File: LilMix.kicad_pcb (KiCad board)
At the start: 2 copper layers, 79.6 x 94.4 mm, 60 parts, among them J1_L1 MONO, J1_R1 MONO, J2_L1 MONO, J2_R1 MONO, J3 STEREO, J4 MONO, J5 MONO, J6 STEREO, U1 TL074, U2 NE5532

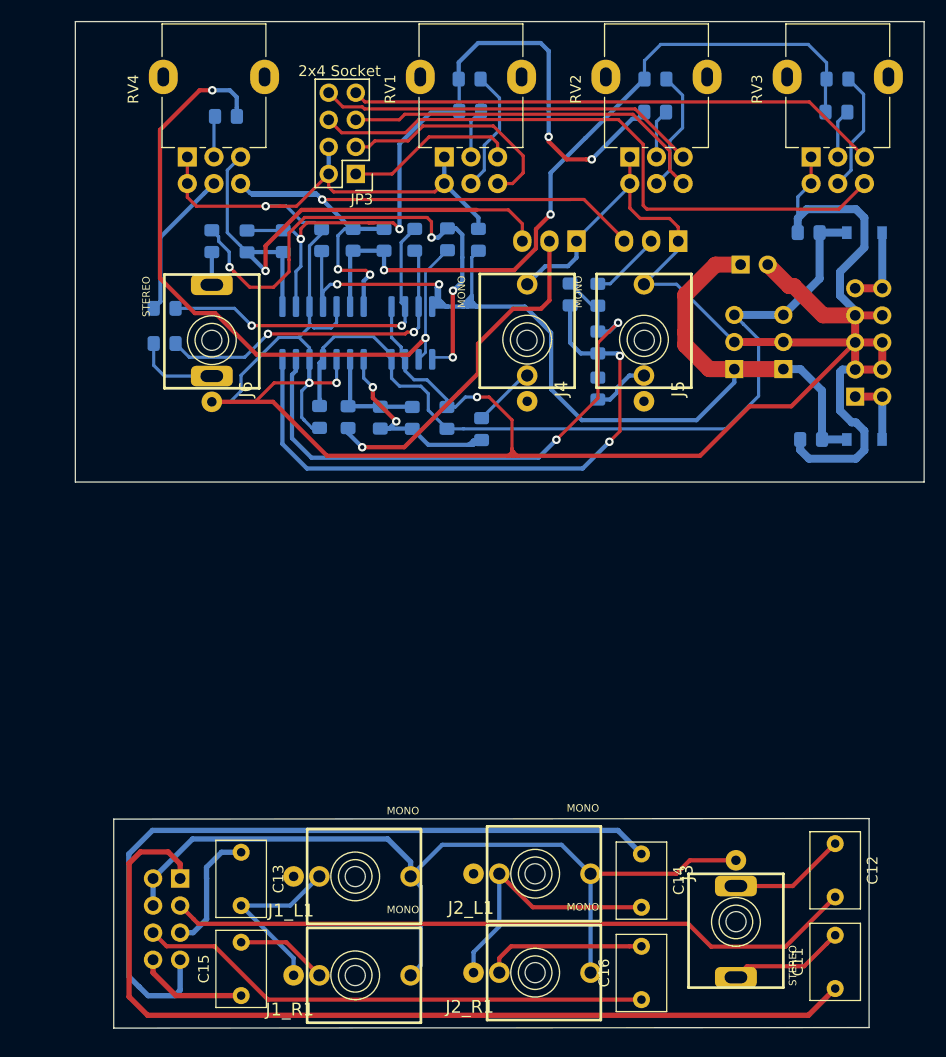
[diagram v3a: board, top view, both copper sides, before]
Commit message: Fixed jack destinatios and flipped front board orientation. Rerouted pcb
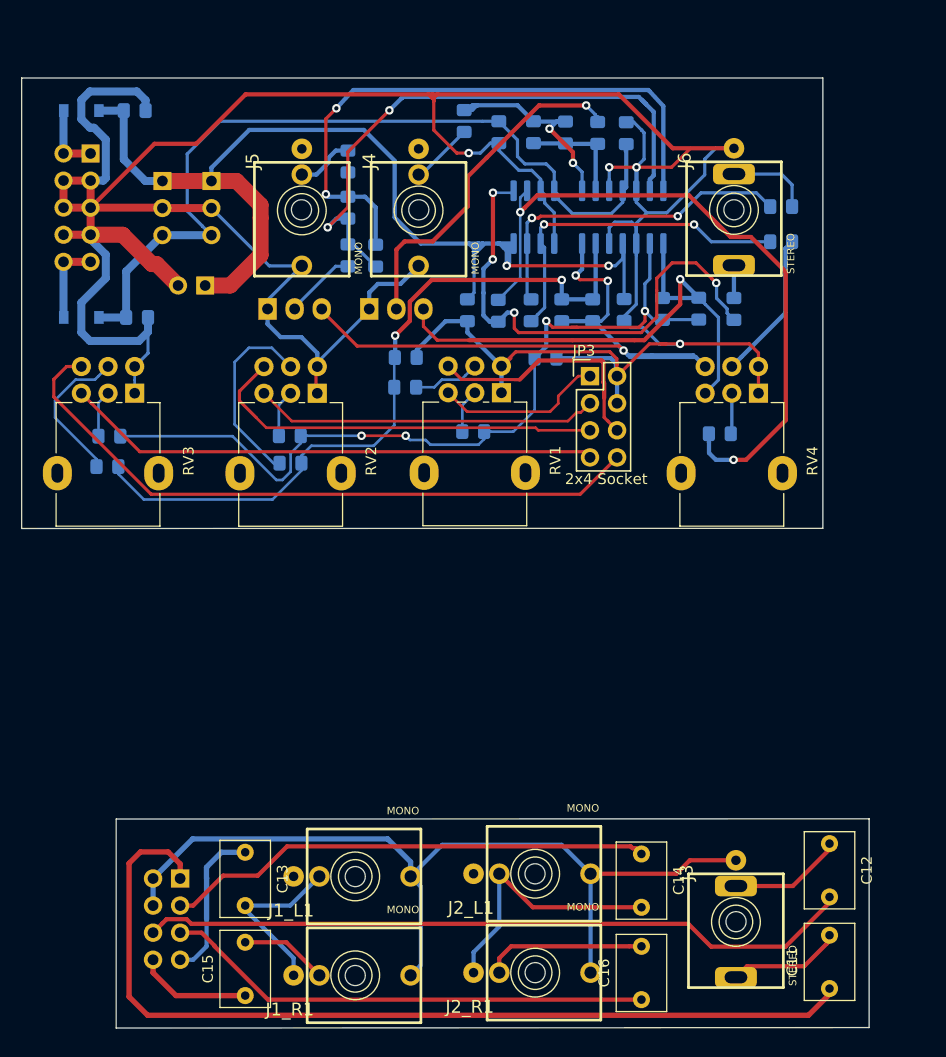
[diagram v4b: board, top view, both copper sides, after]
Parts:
- added R21: 2M, Resistor_SMD:R_0805_2012Metric_Pad1.15x1.40mm_HandSolder, B.Cu at (133.5, 96.2)
- added R22: 2M, Resistor_SMD:R_0805_2012Metric_Pad1.15x1.40mm_HandSolder, B.Cu at (120.4, 96.1)
- moved JP1 81.2 mm to (86.1, 87.7), turned to 180 degrees
- moved D1 79.6 mm to (90.0, 73.0), turned to 180 degrees
- moved D2 73.9 mm to (90.0, 92.4), turned to 0 degrees
- moved C1 70.5 mm to (95.0, 73.0), turned to 0 degrees
- moved RV3 67.2 mm to (95.0, 99.5), turned to 270 degrees
- moved C2 63.5 mm to (95.2, 92.4), turned to 180 degrees
- moved R4 62.9 mm to (92.4, 106.3), turned to 180 degrees
- moved R5 60.9 mm to (109.6, 106.0), turned to 180 degrees
- moved JP4 60.8 mm to (97.6, 79.6), turned to 180 degrees
- moved R20 59.2 mm to (155.6, 82.0), turned to 180 degrees
- moved R10 58.2 mm to (155.6, 85.3), turned to 0 degrees
- moved RV4 58.0 mm to (153.5, 99.5), turned to 270 degrees
- moved R9 55.1 mm to (149.8, 103.3), turned to 0 degrees
- moved JP5 52.1 mm to (102.2, 79.6), turned to 180 degrees
- moved J6 50.5 mm to (151.2, 82.3), turned to 90 degrees
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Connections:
- JP2 pad 3: J3_R_B -> J2_L_B
- JP2 pad 5: J1_L_B -> J2_R_B
- JP2 pad 6: J2_R_B -> J3_R_B
- JP2 pad 7: J2_L_B -> J1_L_B
- JP3 pad 1: J1_L_A -> J3_L_A
- JP3 pad 5: J1_R_A -> J2_R_A
- JP3 pad 7: J2_R_A -> J1_L_A
- JP3 pad 8: J3_L_A -> J1_R_A
- RV1 pad 2: Net-(R1-Pad2) -> Net-(R3-Pad2)
- RV1 pad 3: J1_L_A -> J3_L_A
- RV1 pad 5: Net-(R2-Pad2) -> Net-(R6-Pad2)
- RV1 pad 6: J2_L_A -> J3_R_A
- RV2 pad 2: Net-(R3-Pad2) -> Net-(R2-Pad2)
- RV2 pad 3: J3_L_A -> J2_L_A
- RV2 pad 5: Net-(R4-Pad2) -> Net-(R5-Pad2)
- RV2 pad 6: J1_R_A -> J2_R_A
- RV3 pad 2: Net-(R5-Pad2) -> Net-(R1-Pad2)
- RV3 pad 3: J2_R_A -> J1_L_A
- RV3 pad 5: Net-(R6-Pad2) -> Net-(R4-Pad2)
- RV3 pad 6: J3_R_A -> J1_R_A
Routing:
- net J3_R_A: track 59.1 -> 22.8 mm
- net J1_L_A: track 16.3 -> 50.2 mm
- net J1_R_A: track 34.7 -> 62.8 mm
- net J2_L_B: track 70.0 -> 45.9 mm
- net J3_L_A: track 35.7 -> 15.8 mm
- net GND: track 319.0 -> 334.3 mm
- net Net-(R5-Pad2): track 4.57 -> 18.1 mm
- net J2_R_A: track 50.2 -> 38.2 mm
- net J2_L_A: track 22.1 -> 32.4 mm
- net Net-(R2-Pad2): track 11.6 -> 4.44 mm
- net Net-(C6-Pad2): track 73.1 -> 78.3 mm
- net Net-(R6-Pad2): track 11.4 -> 6.32 mm
- net Net-(R11-Pad2): track 42.7 -> 39.8 mm
- net Net-(R4-Pad2): track 11.4 -> 14.1 mm
- net J1_L_B: track 11.7 -> 14.3 mm
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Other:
- board size 79.6 x 94.4 mm -> 79.5 x 89.1 mm

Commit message: Components moved, board wiring needs to be redone. Removed trim pots on line out. Replaced jacks on large board
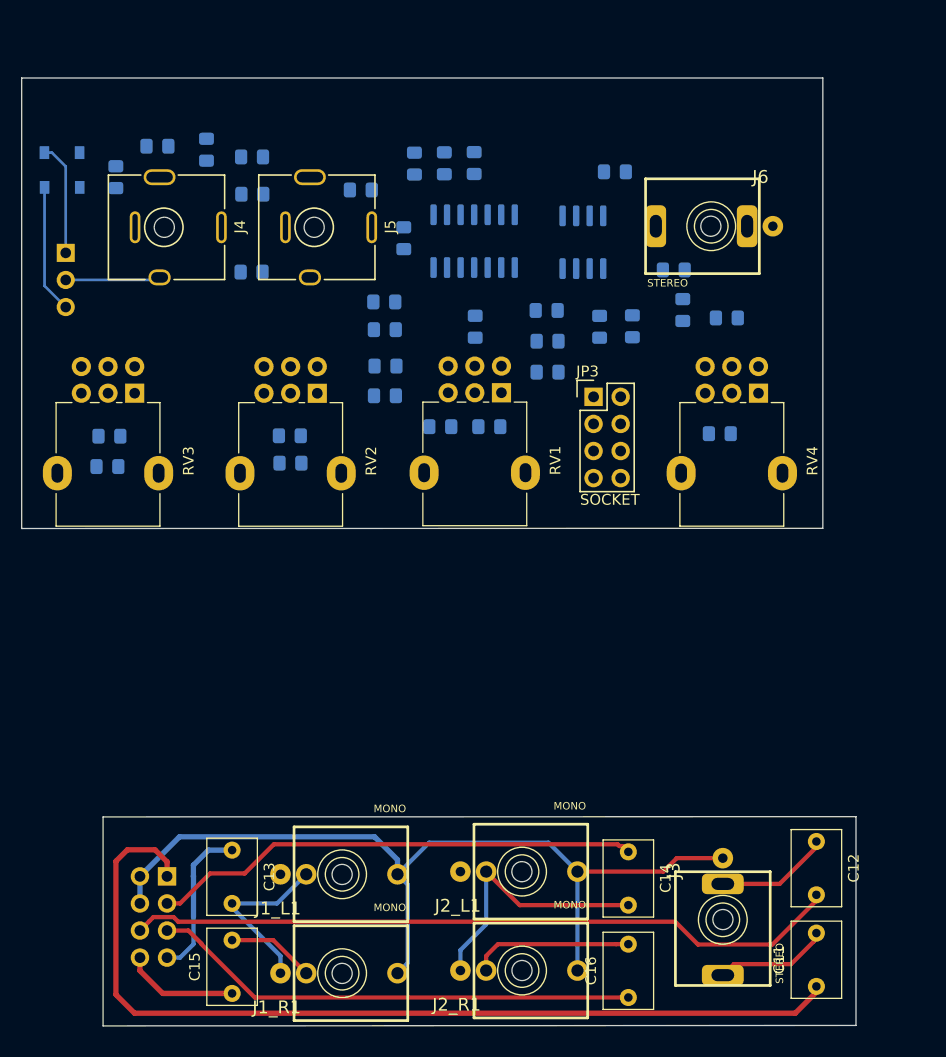
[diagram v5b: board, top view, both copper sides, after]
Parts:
- removed the JP1 at (86.1, 87.7)
- removed JP5: Conn_01x03, Connector_PinSocket_2.54mm:PinSocket_1x03_P2.54mm_Vertical
- removed JP6: Conn_01x02, Connector_PinSocket_2.54mm:PinSocket_1x02_P2.54mm_Vertical
- removed RV5, RV6: 100k, 4ms-footprints:Audio_Mod_Header_1x03
- J4, J5: footprint 4ms-footprints:PJ301M-12 -> Eurocad:EighthInch_PJ301BM_CC_FIXED
- JP1: renamed from JP4; value Conn_01x03 -> PINS
- JP2, JP3: value 2x4 Socket -> SOCKET
- moved R7 29.5 mm to (118.4, 93.5), turned to 0 degrees
- moved J4 26.6 mm to (95.0, 83.9), turned to 270 degrees
- moved C6 26.1 mm to (118.4, 90.9), turned to 0 degrees
- moved R17 24.3 mm to (101.7, 76.6)
- moved R11 20.7 mm to (120.2, 84.9), turned to 270 degrees
- moved C2 16.2 mm to (97.1, 76.3)
- moved D2 15.6 mm to (88.2, 76.9)
- moved R16 14.8 mm to (106.0, 77.3), turned to 0 degrees
- moved C9 14.5 mm to (121.2, 77.9), turned to 90 degrees
- moved U1 14.1 mm to (126.8, 85.2)
- moved R20 11.7 mm to (145.5, 87.9)
- moved JP1 11.3 mm to (88.5, 86.3)
- moved R13 9.62 mm to (138.6, 93.2)
- moved R14 9.62 mm to (141.6, 93.2)
- moved R12 9.17 mm to (105.9, 88.1), turned to 180 degrees
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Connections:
- D1 pad 2: Net-(D1-Pad2) -> +12V_in
- D2 pad 1: Net-(D2-Pad1) -> -12V_in
- JP1 pad 1: +12V -> -12V_in
- JP1 pad 3: -12V -> +12V_in
- R11 pad 2: Net-(R11-Pad2) -> L_INV
- R12 pad 2: Net-(R12-Pad2) -> R_INV
- U1 pad 1: L_INV -> R_INV
- U1 pad 2: Net-(C6-Pad2) -> Net-(C7-Pad2)
- U1 pad 6: Net-(C7-Pad2) -> Net-(C6-Pad2)
- U1 pad 7: R_INV -> L_INV
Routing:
- net GND: track 334.3 -> 8.90 mm, vias 4 -> 0
- net +12V: track 106.0 -> 0.00 mm, vias 2 -> 0
- net -12V: track 79.4 -> 0.00 mm
- net Net-(C6-Pad2): track 78.3 -> 0.00 mm, vias 4 -> 0
- net Net-(C7-Pad2): track 68.6 -> 0.00 mm, vias 2 -> 0
- net R_INV: track 64.8 -> 0.00 mm, vias 3 -> 0
- net Net-(R13-Pad2): track 64.6 -> 0.00 mm, vias 2 -> 0
- net J1_R_A: track 62.8 -> 0.00 mm
- net Net-(C10-Pad1): track 59.4 -> 0.00 mm, vias 2 -> 0
- net Net-(C10-Pad2): track 55.6 -> 0.00 mm, vias 2 -> 0
- net L_INV: track 51.2 -> 0.00 mm, vias 1 -> 0
- net J1_L_A: track 50.2 -> 0.00 mm
- net Net-(R13-Pad1): track 47.7 -> 0.00 mm, vias 4 -> 0
- net Net-(R11-Pad2): track 39.8 -> 0.00 mm, vias 1 -> 0
- net J2_R_A: track 38.2 -> 0.00 mm
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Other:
- board size 79.5 x 89.1 mm -> 78.2 x 88.9 mm

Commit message: Finished initial routing
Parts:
- moved R14 15.0 mm to (145.7, 78.8), turned to 180 degrees
- moved C1 5.89 mm to (88.5, 82.7), turned to 180 degrees
- moved R20 4.99 mm to (148.4, 92.0)
- moved R10 4.90 mm to (146.9, 89.0)
- moved R16 4.28 mm to (106.2, 81.6), turned to 180 degrees
- moved C2 3.77 mm to (93.7, 77.9), turned to 90 degrees
- moved R19 3.69 mm to (142.7, 92.3)
- moved C10 1.99 mm to (106.2, 78.8), turned to 180 degrees
- moved R17 1.48 mm to (101.9, 78.1)
- moved R13 1.39 mm to (139.5, 92.2)
- moved C4 0.87 mm to (126.8, 92.4)
- moved C8 0.70 mm to (133.9, 91.1)
- moved U1 0.17 mm to (126.8, 85.4)
- turned C3 to 90 degrees
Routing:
- net GND: track 8.90 -> 239.2 mm, vias 0 -> 4
- net Net-(C6-Pad2): track 0.00 -> 69.6 mm
- net Net-(C7-Pad2): track 0.00 -> 68.7 mm, vias 0 -> 2
- net +12V: track 0.00 -> 65.5 mm
- net -12V: track 0.00 -> 63.4 mm
- net J1_R_A: track 0.00 -> 62.0 mm
- net R_INV: track 0.00 -> 58.9 mm, vias 0 -> 3
- net J1_L_A: track 0.00 -> 51.3 mm
- net L_INV: track 0.00 -> 51.3 mm, vias 0 -> 1
- net Net-(C10-Pad2): track 0.00 -> 41.5 mm, vias 0 -> 2
- net J2_R_A: track 0.00 -> 39.3 mm
- net Net-(C10-Pad1): track 0.00 -> 35.7 mm, vias 0 -> 2
- net J2_L_A: track 0.00 -> 32.1 mm
- net Net-(R13-Pad2): track 0.00 -> 28.9 mm
- net Net-(C9-Pad1): track 0.00 -> 28.8 mm
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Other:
- board size 78.2 x 88.9 mm -> 78.3 x 84.4 mm

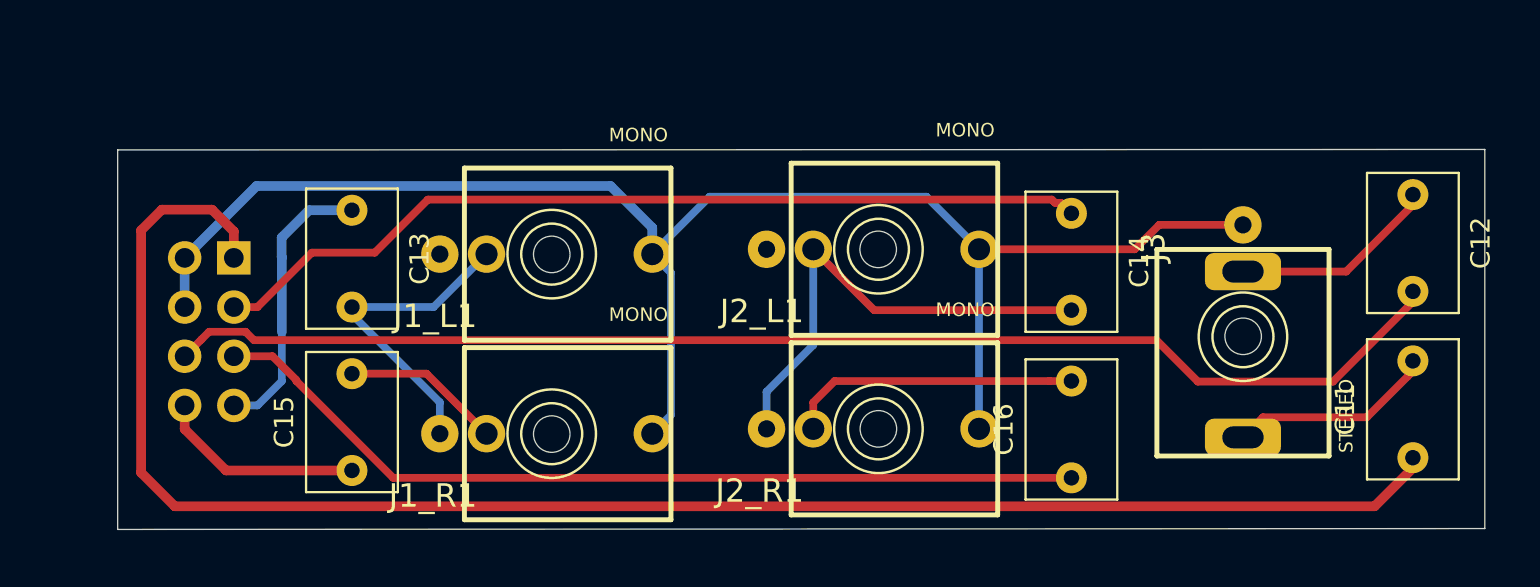
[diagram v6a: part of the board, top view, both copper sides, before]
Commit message: Removed extra jack connection from schematic. Added second jack to 3rd channel. Repositioned jack board for even space between jacks, with slightly reduced overall dimensions
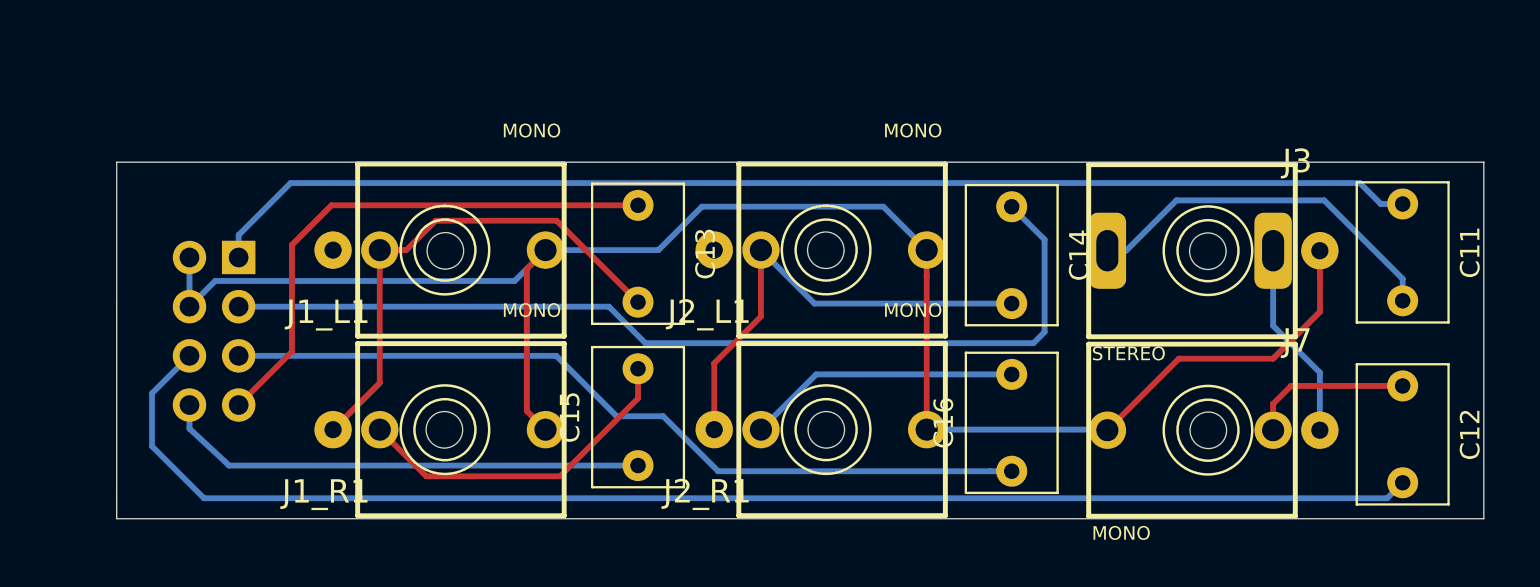
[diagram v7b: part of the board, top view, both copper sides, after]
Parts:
- added J7: MONO, 4ms-footprints:PJ301M-12, F.Cu at (148.3, 153.7)
- moved C13 14.8 mm to (118.9, 142.1)
- moved C15 14.8 mm to (118.9, 155.5)
- moved C11 13.1 mm to (158.4, 142.0), turned to 270 degrees
- moved C12 9.90 mm to (158.4, 151.4)
- moved J1_L1 5.52 mm to (108.9, 144.4)
- moved J1_R1 5.52 mm to (108.9, 153.6)
- moved J3 4.78 mm to (148.3, 144.4), turned to 0 degrees
- moved C14 3.10 mm to (138.2, 142.1)
- moved C16 3.10 mm to (138.2, 155.8)
- moved J2_L1 2.70 mm to (128.6, 144.4)
- moved J2_R1 2.70 mm to (128.6, 153.6)
- moved JP2 0.25 mm to (98.2, 144.8)
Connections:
- J3 pad 3: Net-(C12-Pad1) -> J7_INSERT
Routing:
- net J3_L_B: track 87.6 -> 62.8 mm
- net J1_R_B: track 10.4 -> 25.1 mm
- net J1_L_B: track 14.3 -> 28.1 mm
- net J7_INSERT: track 0.00 -> 10.3 mm
- net J1_INSERT: track 17.0 -> 26.0 mm
- net Net-(C15-Pad2): track 8.62 -> 17.5 mm
- net Net-(C11-Pad2): track 10.9 -> 19.1 mm
- net GND_B: track 83.2 -> 89.0 mm
- net J3_R_B: track 67.5 -> 71.5 mm
- net J2_L_B: track 45.9 -> 49.8 mm
- net J2_R_B: track 45.9 -> 42.4 mm
- net Net-(C12-Pad1): track 11.0 -> 8.44 mm
- net Net-(C16-Pad2): track 15.2 -> 14.1 mm
- net J2_INSERT: track 24.9 -> 24.4 mm
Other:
- board size 78.3 x 84.4 mm -> 78.2 x 83.9 mm

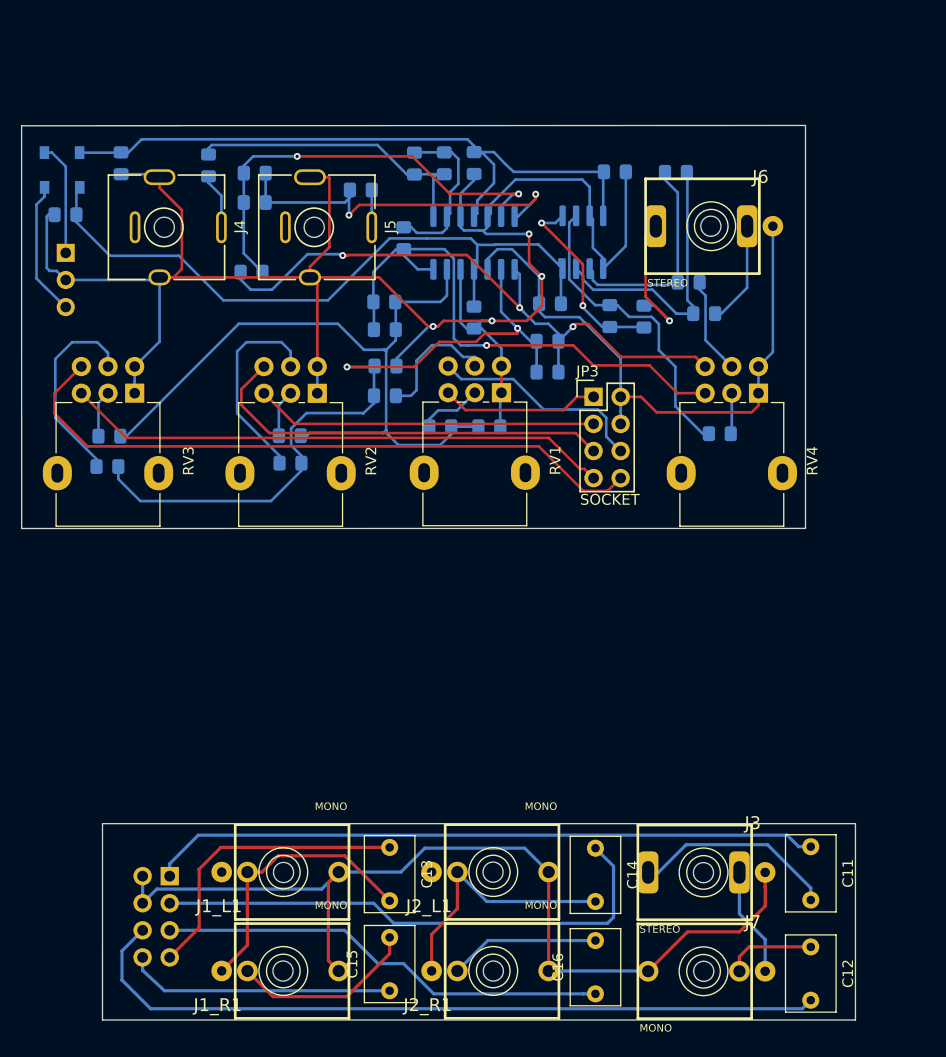
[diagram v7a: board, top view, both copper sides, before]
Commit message: Fixed J7 insert
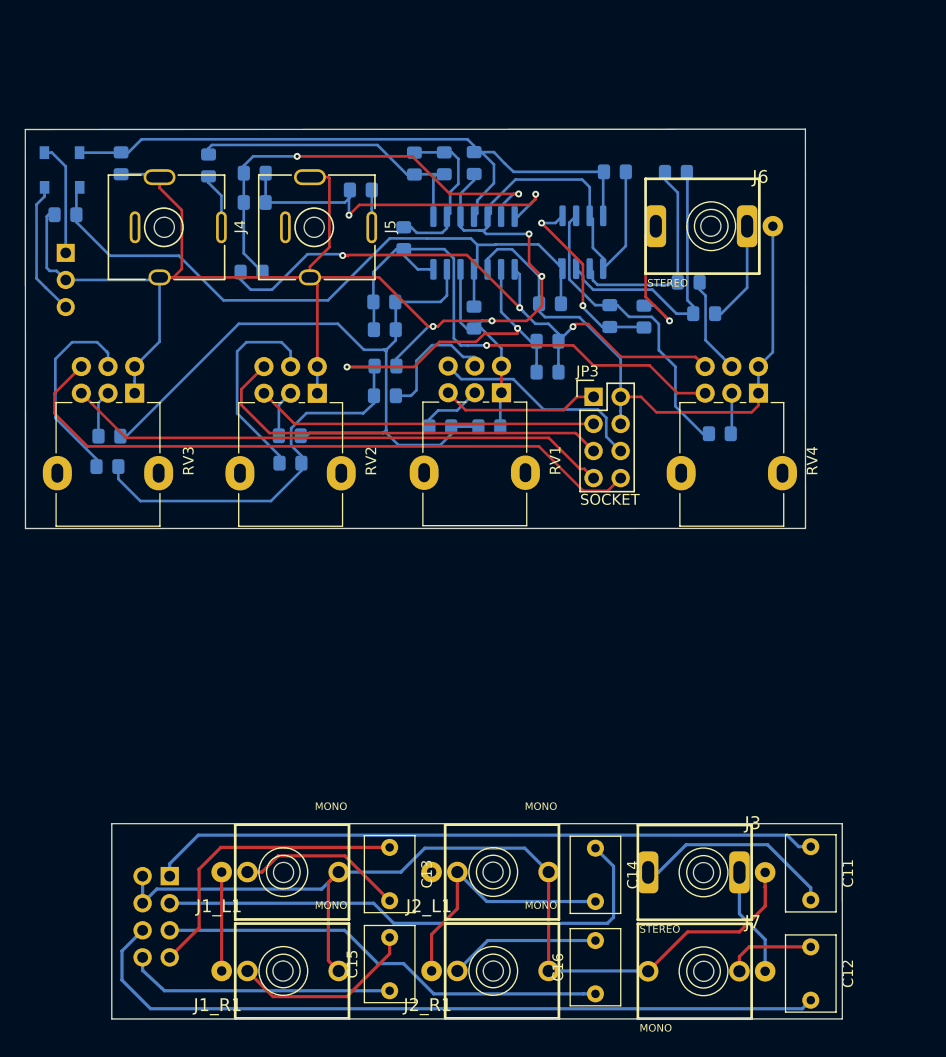
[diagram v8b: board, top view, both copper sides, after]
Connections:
- C13 pad 2: J1_INSERT -> Net-(C13-Pad2)
- J1_L1 pad 2: Net-(J1_L1-Pad2) -> J1_INSERT
- J1_L1 pad 3: J1_INSERT -> Net-(C13-Pad2)
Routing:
- net J1_INSERT: track 26.0 -> 9.28 mm
- net Net-(C13-Pad2): track 0.00 -> 15.7 mm
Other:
- board size 78.2 x 83.9 mm -> 76.6 x 83.4 mm
